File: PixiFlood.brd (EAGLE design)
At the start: 45 x 47 mm, 34 parts, among them IC1 TC7W04FP-0.65, IC2 WS2811SOP8, IC3 78L05Z, U1 PT4115B89E, U2 PT4115B89E, U3 PT4115B89E, X1 22-23-2031, X2 22-23-2031

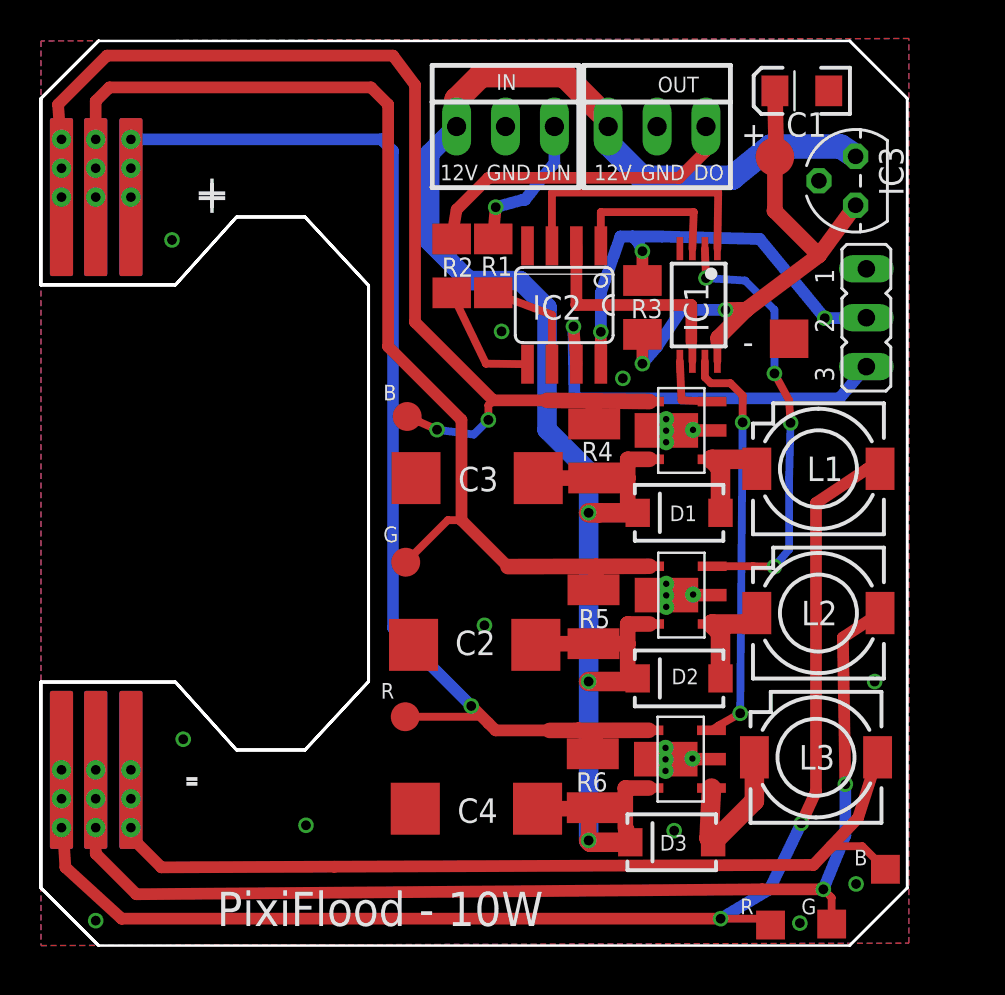
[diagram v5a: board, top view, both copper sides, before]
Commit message: Reworked layout
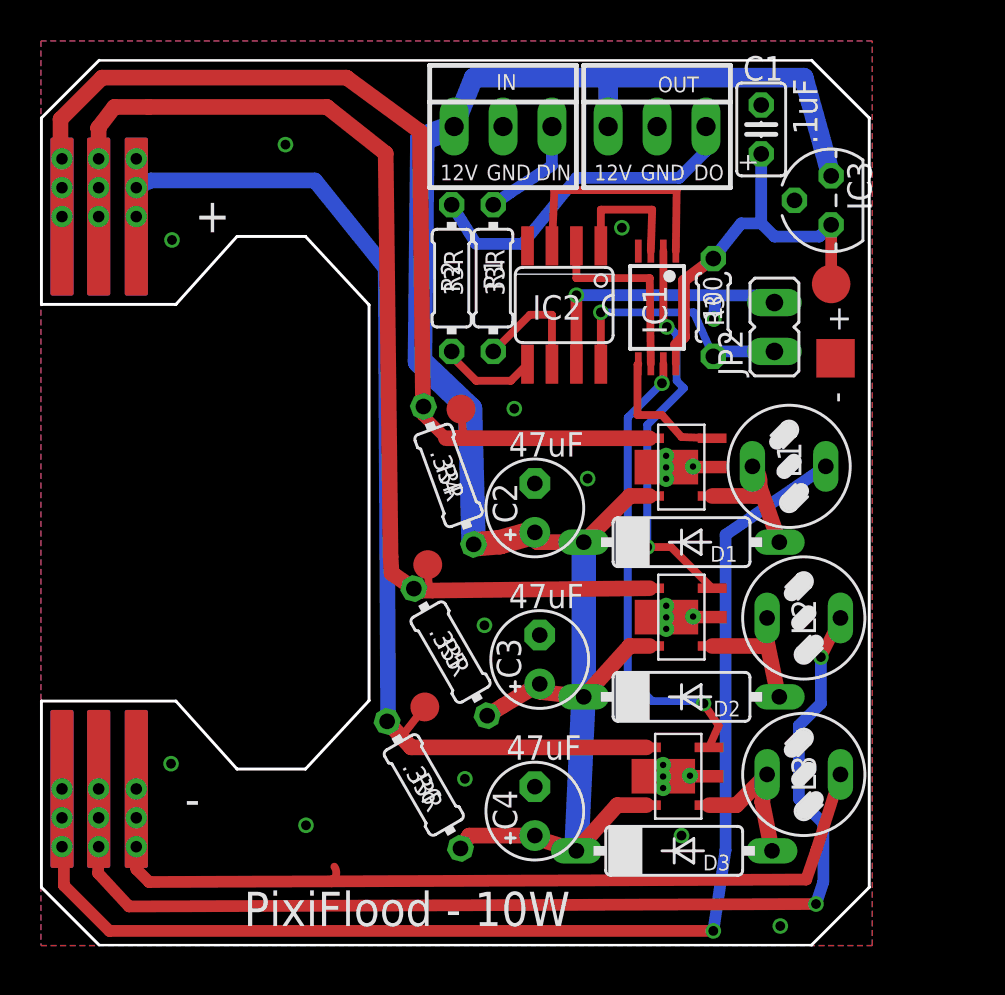
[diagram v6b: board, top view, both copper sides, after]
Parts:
- removed JP1: (no value), jumper:JP2
- removed TP6, TP8, TP9: TPSQTP15SQ, testpad:TP15SQ
- added JP2: (no value), jumper:JP1
- B1: value LED-BOARDV2 -> LED-BOARDV3; device special:LED-BOARD_V2 -> special:LED-BOARD_V3
- C1: device capacitors:EIA3216 -> capacitors:C025X050P
- C2, C3, C4: value 10uF -> 47uF; device capacitors:D/7343-31R -> adafruit:E2,5-5
- D1, D2, D3: value MBRA140 -> 1N5819; device SparkFun-DiscreteSemi:SMA-DIODE -> diode:DO07
- L1, L2, L3: value SLF7045T-101MR60-H -> 82114R; device inductors:SLF7045 -> inductors:82114R
- R1, R2: device rcl:M1206 -> rcl:0204/7
- R3: value 100ohm -> 100; device rcl:M1206 -> rcl:0204/5
- R4, R6: value .3ohm .25w -> .33R; device resistor:R1210 -> resistor:0204/7
- R5: value .3hm .25w -> .33R; device resistor:R1210 -> resistor:0204/7
- moved C3 9.97 mm to (25.9, 14.9), turned to 90 degrees
- moved R6 8.78 mm to (19.9, 8.35), turned to 300 degrees
- moved C2 7.77 mm to (25.7, 22.7), turned to 90 degrees
- moved R4 7.67 mm to (21.2, 24.4), turned to 290 degrees
- moved R5 7.65 mm to (21.3, 15.2), turned to 300 degrees
- moved TP1 7.22 mm to (41.0, 34.4)
- moved R3 3.68 mm to (34.9, 33.1), turned to 270 degrees
- moved C4 3.04 mm to (25.7, 6.99), turned to 90 degrees
- moved C1 2.91 mm to (37.4, 42.4), turned to 90 degrees
- moved TP3 2.82 mm to (21.8, 27.9)
- moved TP2 2.62 mm to (41.3, 30.5)
- moved IC1 2.16 mm to (32.0, 33.1)
- moved U1 1.91 mm to (33.3, 24.9)
- moved IC3 1.63 mm to (41.0, 38.7)
- moved D1 1.53 mm to (33.3, 21.0), turned to 0 degrees
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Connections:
- removed net N$18: IC2.7, JP1.3
- new net N$17: IC2.7, JP2.2
- net +5V: now also C1.1; no longer C1.A
- net BOUT: now also B1.B+@1, B1.B+@2, B1.B+@3; no longer B1.P$5@1, B1.P$5@2, B1.P$5@3
- net GND: now also C1.2; no longer C1.C
- net GOUT: now also B1.G+@1, B1.G+@2, B1.G+@3; no longer B1.P$3@1, B1.P$3@2, B1.P$3@3
- net N$10: now also B1.B-@1, B1.B-@2, B1.B-@3; no longer B1.P$6@1, B1.P$6@2, B1.P$6@3, TP6.TP
- net N$14: now also JP2.1; no longer JP1.2
- net N$3: now also B1.R-@1, B1.R-@2, B1.R-@3; no longer B1.P$2@1, B1.P$2@2, B1.P$2@3, TP9.TP
- net N$9: now also B1.G-@1, B1.G-@2, B1.G-@3; no longer B1.P$4@1, B1.P$4@2, B1.P$4@3, TP8.TP
- net ROUT: now also B1.R+@1, B1.R+@2, B1.R+@3; no longer B1.P$1@1, B1.P$1@2, B1.P$1@3
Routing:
- net N$18: track 21.6 -> 0.00 mm, vias 1 -> 0
- net N$17: track 0.00 -> 15.2 mm, vias 0 -> 2
- net N$14: track 24.0 -> 13.3 mm, vias 3 -> 1
- net +5V: track 29.2 -> 20.6 mm, vias 2 -> 0
- net BOUT: track 63.6 -> 58.8 mm, vias 1 -> 0
- net N$10: track 49.6 -> 45.8 mm
- net N$3: track 70.3 -> 66.7 mm, vias 2 -> 1
- net ROUT: track 58.4 -> 54.8 mm, vias 2 -> 0
- net RED: track 3.62 -> 7.07 mm
- net BLUE: track 21.4 -> 24.2 mm
- net +12V: track 103.6 -> 101.0 mm, vias 3 -> 0
- net N$1: track 5.49 -> 7.93 mm
- net N$19: track 12.0 -> 9.94 mm
- net GOUT: track 59.9 -> 57.9 mm
- net N$9: track 60.6 -> 58.6 mm
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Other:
- board size 45 x 47 mm -> 43 x 46 mm
- board text added: "v1.5"
- board text removed: "B"
- board text removed: "G"
- board text removed: "R"
- board text removed: "V1.4"

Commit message: Reworked layout
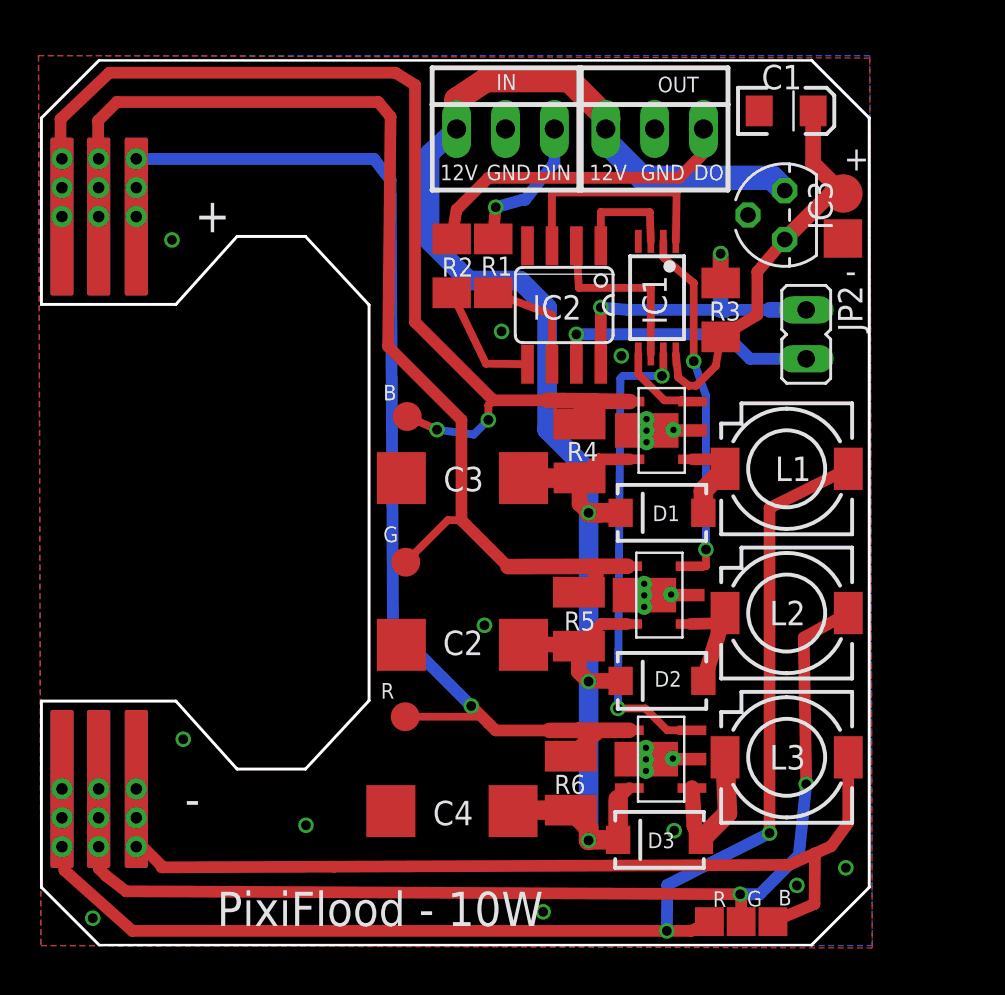
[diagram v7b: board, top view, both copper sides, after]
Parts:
- added TP6, TP8, TP9: TPSQTP15SQ, testpad:TP15SQ
- C1: device capacitors:C025X050P -> capacitors:EIA3216
- C2, C3, C4: value 47uF -> 10uF; device adafruit:E2,5-5 -> capacitors:D/7343-31R
- D1, D2, D3: value 1N5819 -> MBRA140; device diode:DO07 -> SparkFun-DiscreteSemi:SMA-DIODE
- L1, L2, L3: value 82114R -> SLF7045T-101MR60-H; device inductors:82114R -> inductors:SLF7045
- R1, R2: device rcl:0204/7 -> rcl:M1206
- R3: value 100 -> 100ohm; device rcl:0204/5 -> rcl:M1206
- R4, R6: value .33R -> .3ohm .25w; device resistor:0204/7 -> resistor:R1210
- R5: value .33R -> .3hm .25w; device resistor:0204/7 -> resistor:R1210
- moved C3 10.2 mm to (21.9, 24.3), turned to 0 degrees
- moved C2 8.04 mm to (21.9, 15.6), turned to 0 degrees
- moved R6 7.64 mm to (27.5, 8.43), turned to 270 degrees
- moved R4 6.92 mm to (28.0, 25.7), turned to 270 degrees
- moved R5 6.88 mm to (27.9, 17.0), turned to 270 degrees
- moved TP2 6.23 mm to (41.7, 36.7)
- moved TP1 4.74 mm to (41.7, 39.1)
- moved C4 4.30 mm to (21.4, 6.99), turned to 0 degrees
- moved TP3 2.82 mm to (19.0, 27.5)
- moved IC3 2.53 mm to (38.6, 37.9)
- moved U1 2.16 mm to (32.3, 26.8)
- moved D1 1.83 mm to (32.3, 22.5), turned to 180 degrees
- moved JP2 1.69 mm to (39.8, 31.8), turned to 180 degrees
- moved U2 1.62 mm to (32.1, 18.3)
- moved C1 1.62 mm to (38.7, 43.4), turned to 0 degrees
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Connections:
- net +5V: now also C1.A; no longer C1.1
- net GND: now also C1.C; no longer C1.2
- net N$10: now also TP6.TP
- net N$3: now also TP9.TP
- net N$9: now also TP8.TP
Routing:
- net +12V: track 101.0 -> 93.2 mm, vias 0 -> 3
- net N$14: track 13.3 -> 18.3 mm, vias 1 -> 2
- net N$10: track 45.8 -> 49.7 mm
- net N$3: track 66.7 -> 70.4 mm, vias 1 -> 2
- net N$1: track 7.93 -> 4.65 mm
- net ROUT: track 54.8 -> 58.1 mm, vias 0 -> 2
- net BOUT: track 58.8 -> 61.6 mm, vias 0 -> 1
- net RED: track 7.07 -> 4.43 mm
- net GREEN: track 20.9 -> 18.5 mm
- net N$6: track 5.70 -> 7.45 mm, vias 0 -> 1
- net N$5: track 7.07 -> 5.34 mm
- net N$9: track 58.6 -> 57.2 mm
- net N$7: track 5.07 -> 6.25 mm
- net N$18: track 15.2 -> 14.0 mm, vias 2 -> 1
- net GOUT: track 57.9 -> 59.0 mm
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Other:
- board text added: "B"
- board text added: "G"
- board text added: "R"
- board text added: "V1.4"
- board text removed: "v1.5"

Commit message: Reworked layout
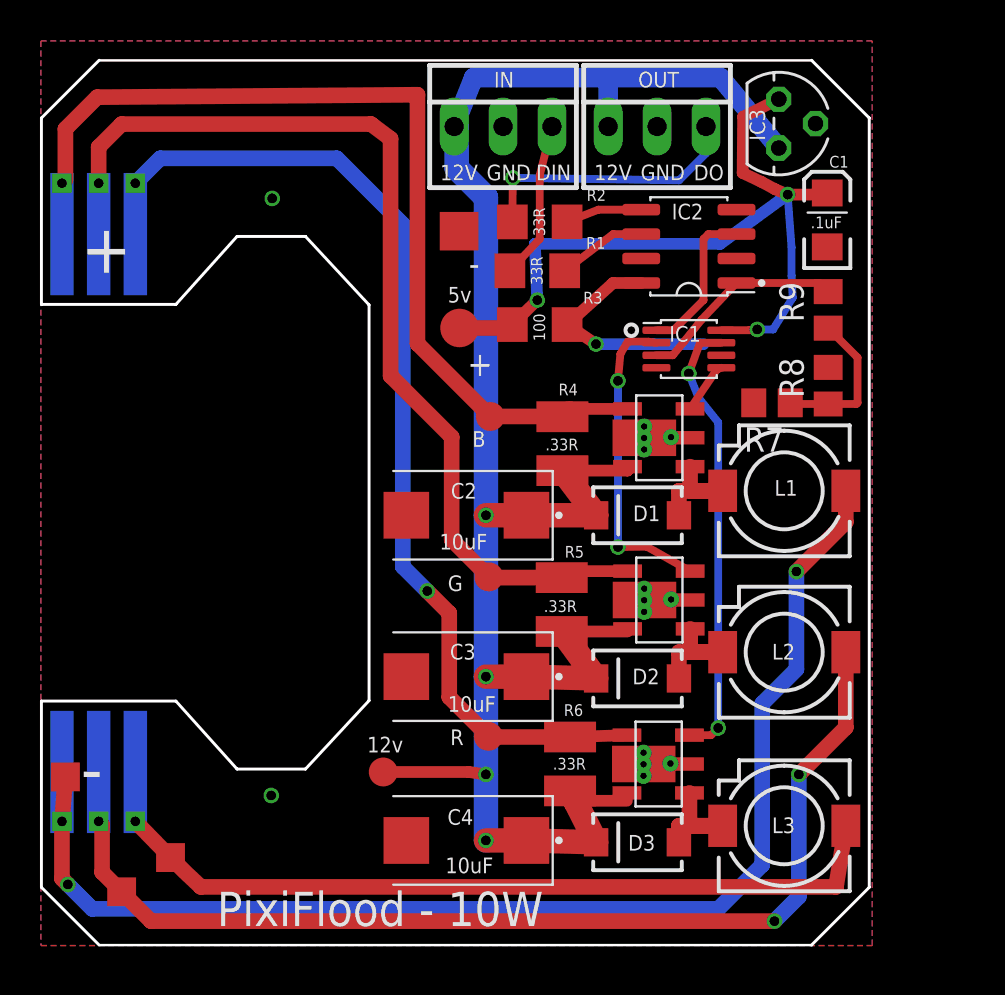
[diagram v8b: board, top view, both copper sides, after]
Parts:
- removed JP2: (no value), jumper:JP1
- added R7, R8, R9: 4.7K, rcl:R0805
- added TP4: TPSQTP15SQ, testpad:TP15SQ
- B1: value LED-BOARDV3 -> LED-BOARDV4; device special:LED-BOARD_V3 -> special:LED_BOARD-V4
- C2, C3, C4: device capacitors:D/7343-31R -> capacitors:VISHAY-CASE-D
- D1, D2, D3: value MBRA140 -> B340A
- IC1: device logic:TSSOP8 -> logic:SSOP8-0.65P
- IC2: value WS2811SOP8 -> WS2811S; device drivers:SOP08-P-1.27 -> drivers:WS2811S
- R1, R2: device rcl:M1206 -> rcl:R1206
- R3: value 100ohm -> 100; device rcl:M1206 -> rcl:R1206
- R4, R6: value .3ohm .25w -> .33R
- R5: value .3hm .25w -> .33R
- TP9: value TPSQTP15SQ -> TPSQTP15R; device testpad:TP15SQ -> testpad:TP15R
- moved TP6 33.9 mm to (4.19, 2.79)
- moved TP8 29.8 mm to (6.73, 4.57)
- moved TP1 21.1 mm to (21.7, 32.1)
- moved TP2 19.9 mm to (21.7, 37.1)
- moved TP9 18.6 mm to (17.8, 9.02)
- moved C3 10.3 mm to (22.1, 14.0)
- moved R3 9.43 mm to (25.9, 32.3), turned to 0 degrees
- moved IC2 7.16 mm to (33.7, 36.3)
- moved C2 6.73 mm to (22.1, 22.4)
- moved C1 6.05 mm to (40.8, 37.7), turned to 90 degrees
- moved R2 5.11 mm to (25.9, 37.6), turned to 0 degrees
- moved IC3 4.76 mm to (38.3, 42.7), turned to 270 degrees
- moved TP7 4.44 mm to (23.2, 10.9)
- moved TP5 4.38 mm to (23.3, 19.2)
- moved TP3 4.32 mm to (23.3, 27.5)
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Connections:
- net +12V: now also C2.1, C3.1, C4.1, TP9.TP; no longer C2.+, C3.+, C4.+
- net BOUT: now also B1.B+; no longer B1.B+@1, B1.B+@3
- net GND: now also C2.2, C3.2, C4.2; no longer C2.-, C3.-, C4.-
- net GOUT: now also B1.G+; no longer B1.G+@2, B1.G+@3
- net N$10: now also B1.B-, TP8.TP; no longer B1.B-@2, B1.B-@3, TP6.TP
- net N$14: no longer JP2.1
- net N$15: now also R9.2
- net N$16: now also R7.2
- net N$18: now also R7.1, R8.1, R9.1; no longer IC2.7, JP2.2
- net N$19: now also R8.2
- net N$3: now also B1.R-, TP4.TP; no longer B1.R-@2, B1.R-@3, TP9.TP
- net N$9: now also B1.G-, TP6.TP; no longer B1.G-@2, B1.G-@3, TP8.TP
- net ROUT: now also B1.R+; no longer B1.R+@2, B1.R+@3
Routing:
- net +5V: track 20.9 -> 41.2 mm, vias 0 -> 3
- net N$19: track 9.36 -> 0.00 mm
- net +12V: track 93.2 -> 101.8 mm, vias 3 -> 4
- net ROUT: track 58.1 -> 50.1 mm, vias 2 -> 0
- net BOUT: track 61.6 -> 54.1 mm
- net GOUT: track 59.0 -> 52.7 mm
- net N$14: track 18.3 -> 12.1 mm, vias 2 -> 1
- net N$10: track 49.7 -> 43.6 mm
- net N$18: track 14.0 -> 8.05 mm, vias 1 -> 0
- net N$15: track 5.81 -> 10.8 mm
- net N$16: track 11.8 -> 8.09 mm
- net N$3: track 70.4 -> 67.1 mm
- net N$4: track 16.9 -> 14.3 mm, vias 0 -> 1
- net N$7: track 6.25 -> 3.97 mm
- net GREEN: track 18.5 -> 16.4 mm
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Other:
- board text added: "12v"
- board text added: "5v"
- board text added: "v1.6"
- board text removed: "V1.4"
